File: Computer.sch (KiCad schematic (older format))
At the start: 42 parts, among them J1 DB9, J2 Screw_Terminal_1x04, U1 8284, U10 74LS04, U11 7400, U12 8259, U13 74LS138, U14 LM7905CT, U15 LM7912CT, U2 LM2931AZ-5.0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

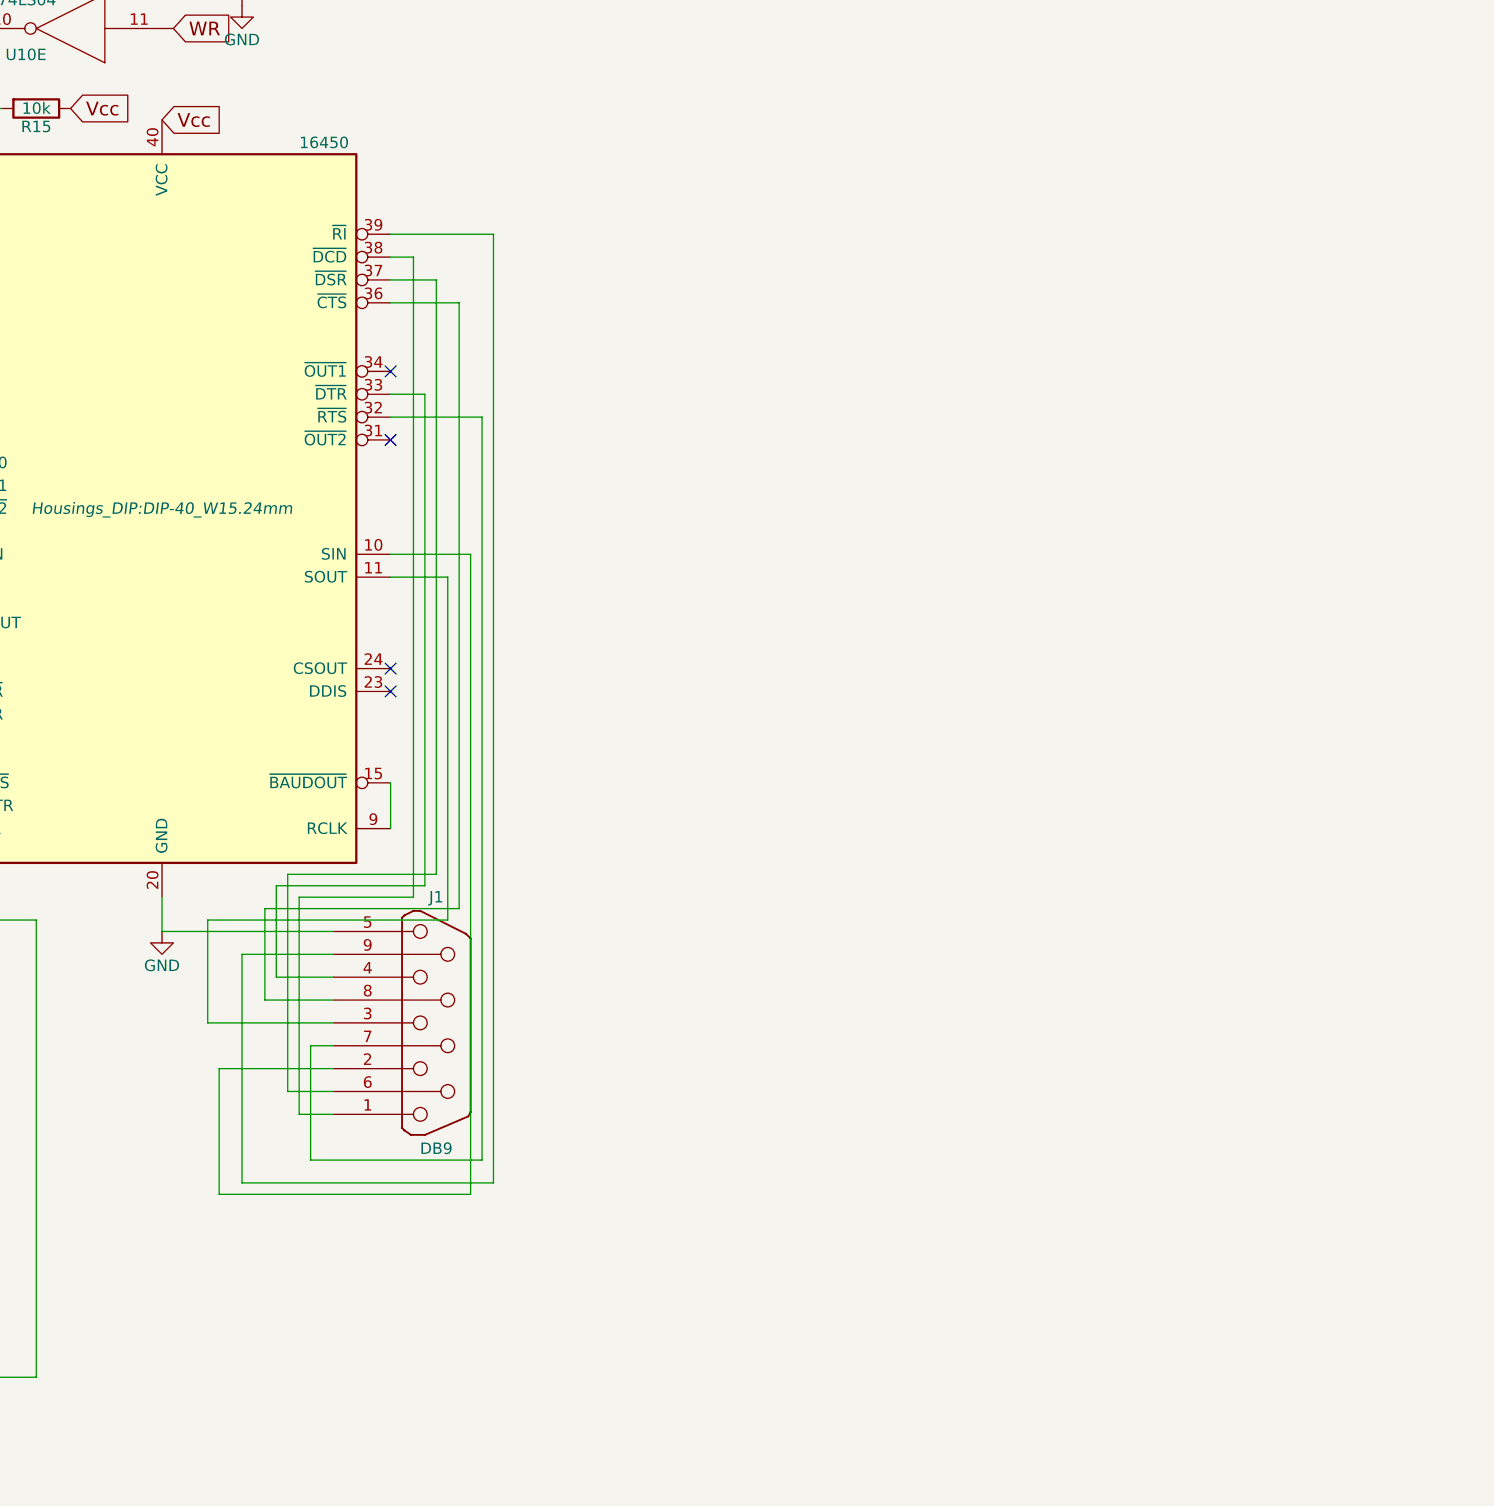
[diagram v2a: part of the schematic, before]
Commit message: Start adding RS232 level shifters
Signed-off-by: Nkeck720 <noahkeck72@gmail.com>
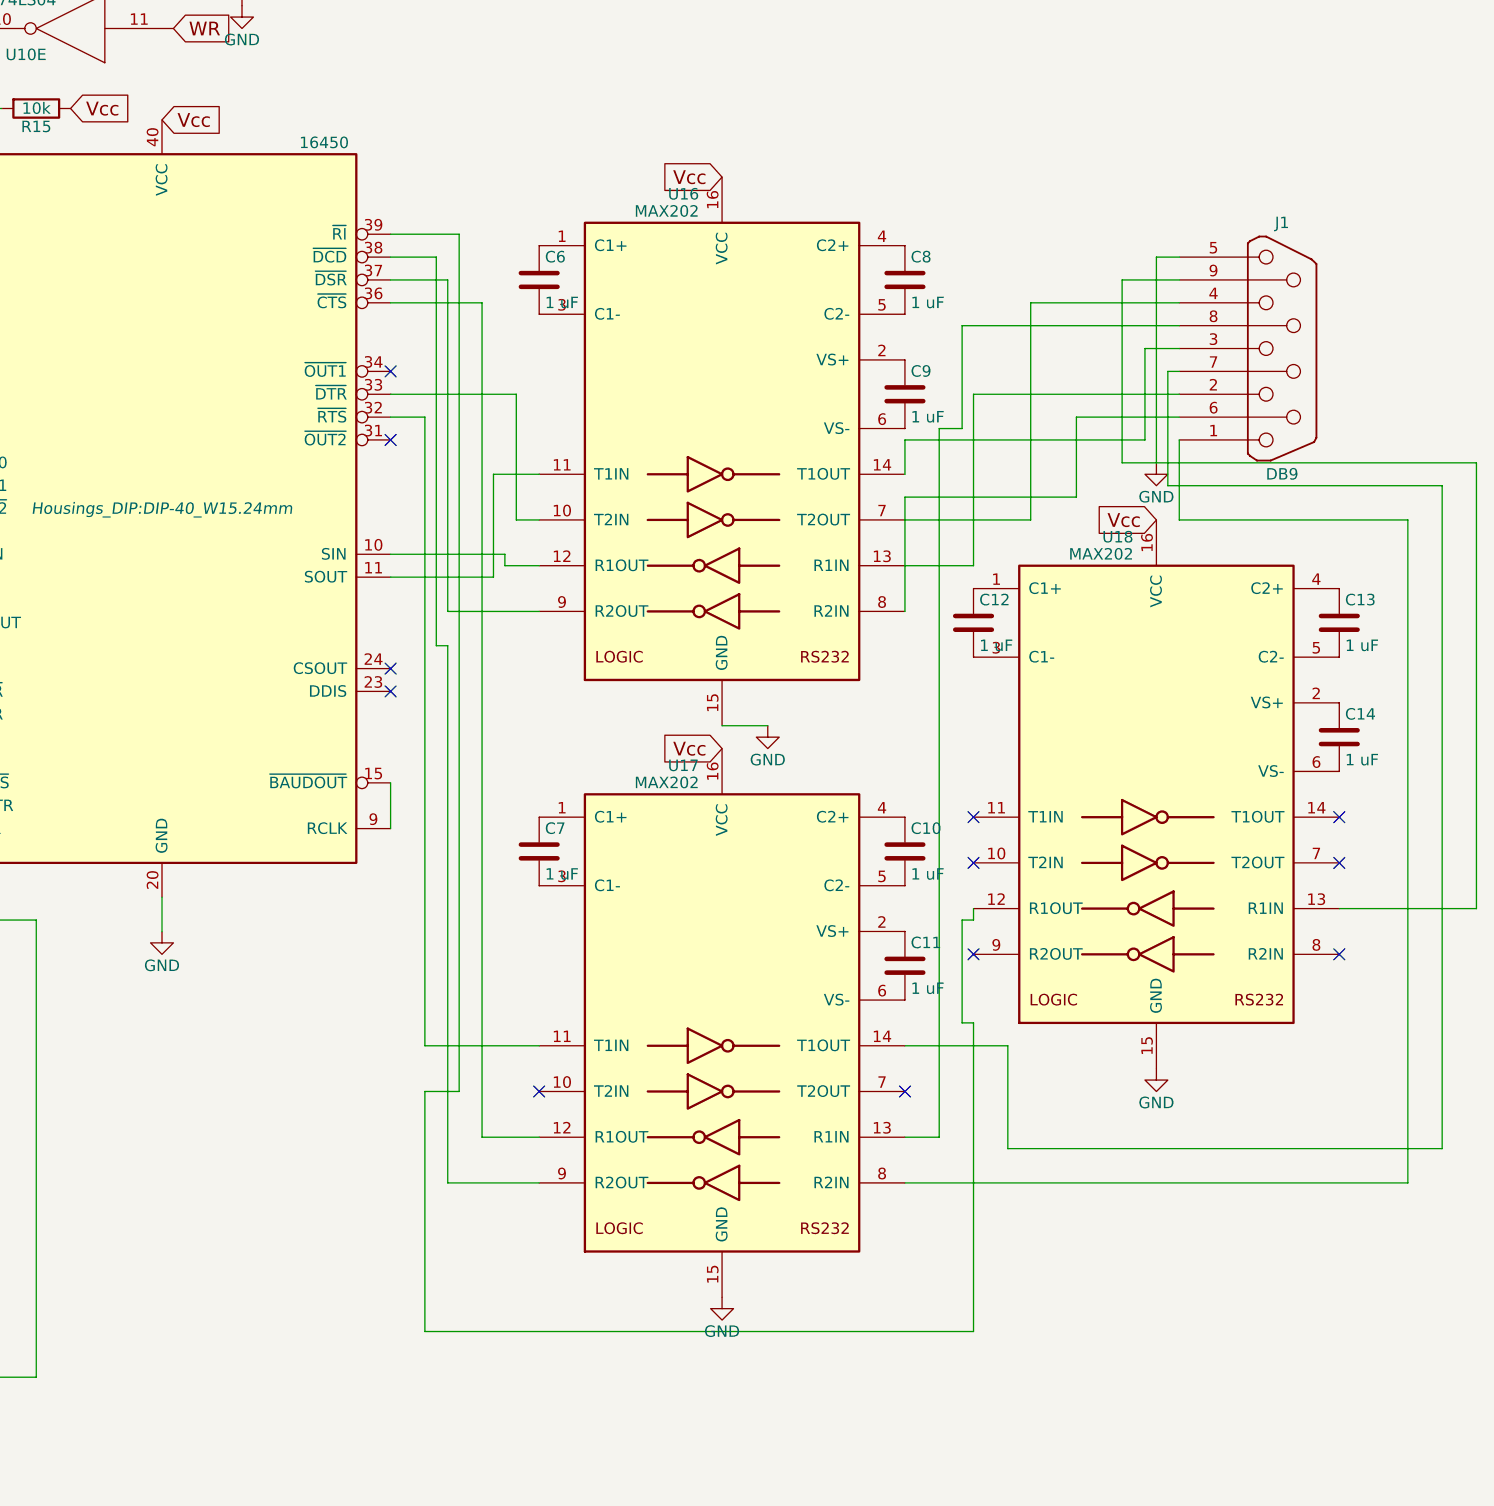
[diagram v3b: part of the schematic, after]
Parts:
- added C10, C11, C12, C13, C14, C6, C7, C8, C9: 1 uF, Capacitors_SMD:C_0603_HandSoldering, symbol C
- added U16, U17, U18: MAX202, Housings_DIP:DIP-16_W7.62mm, symbol MAX202
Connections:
- net GND: now also U16.15 (GND), U17.15 (GND), U18.15 (GND)
- net Vcc: now also U16.16 (VCC), U17.16 (VCC), U18.16 (VCC)
- net at U7.10 (SIN): now also U16.12 (R1OUT); no longer J1.2
- net at U7.11 (SOUT): now also U16.11 (T1IN); no longer J1.3
- net at U7.32 (~RTS~): now also U17.11 (T1IN); no longer J1.7 (P7)
- net at U7.33 (~DTR~): now also U16.10 (T2IN); no longer J1.4
- net at U7.36 (~CTS~): now also U17.12 (R1OUT); no longer J1.8 (P8)
- net at U7.37 (~DSR~): now also U16.9 (R2OUT); no longer J1.6 (P6)
- net at U7.38 (~DCD~): now also U17.9 (R2OUT); no longer J1.1
- net at U7.39 (~RI~): now also U18.12 (R1OUT); no longer J1.9 (P9)
- new net: C6.1, U16.1 (C1+)
- new net: J1.2, U16.13 (R1IN)
- new net: J1.3, U16.14 (T1OUT)
- new net: C9.1, U16.2 (VS+)
- new net: C6.2, U16.3 (C1-)
- new net: C8.1, U16.4 (C2+)
- new net: C8.2, U16.5 (C2-)
- new net: C9.2, U16.6 (VS-)
- new net: J1.4, U16.7 (T2OUT)
- new net: J1.6 (P6), U16.8 (R2IN)
- new net: C12.1, U18.1 (C1+)
- new net: J1.9 (P9), U18.13 (R1IN)
- new net: C14.1, U18.2 (VS+)
- new net: C12.2, U18.3 (C1-)
- new net: C13.1, U18.4 (C2+)
- new net: C13.2, U18.5 (C2-)
- new net: C14.2, U18.6 (VS-)
- new net: C7.1, U17.1 (C1+)
- new net: C7.2, U17.3 (C1-)
- new net: C10.1, U17.4 (C2+)
- new net: C10.2, U17.5 (C2-)
- new net: J1.8 (P8), U17.13 (R1IN)
- new net: J1.7 (P7), U17.14 (T1OUT)
- new net: C11.1, U17.2 (VS+)
- new net: C11.2, U17.6 (VS-)
- new net: J1.1, U17.8 (R2IN)
- no-connect marks 42 -> 50
